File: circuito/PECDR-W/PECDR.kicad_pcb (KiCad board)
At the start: 4 copper layers, 85 x 54 mm, 68 parts, among them J1 O2, J10 GP-SPI, J11 GP-SPI, J12 O3, J13 GND, J14 A, J15 B, J16 VS-SELECT, J17 GP-I2C1, J2 O4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

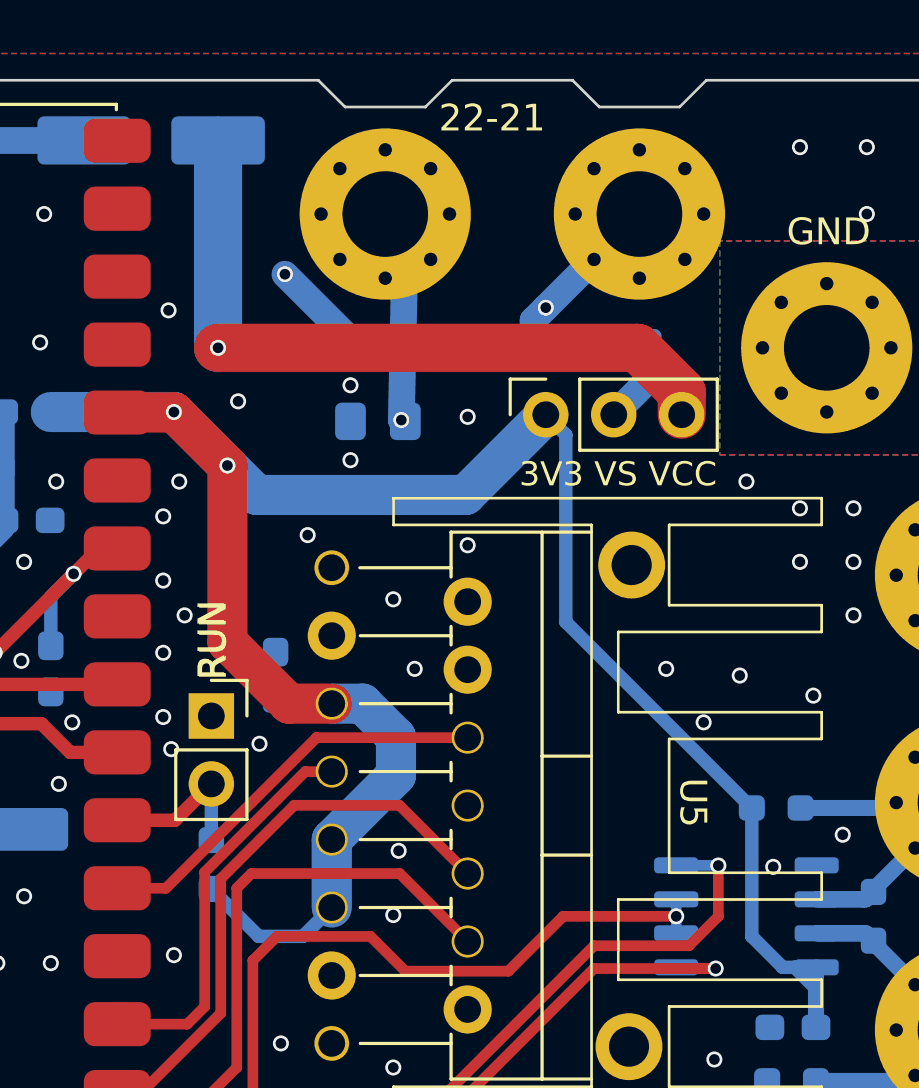
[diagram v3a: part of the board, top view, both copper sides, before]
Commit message: correção de layout e conexões no circuito PECDR-W
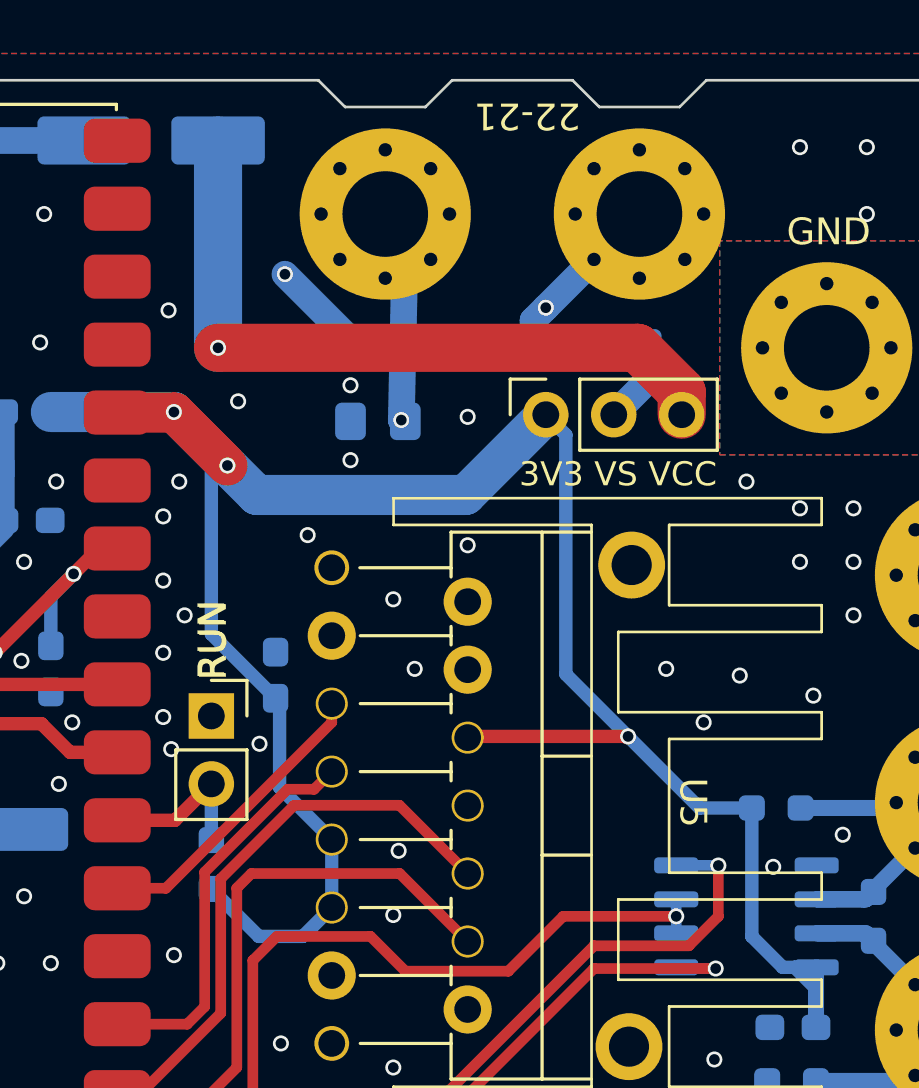
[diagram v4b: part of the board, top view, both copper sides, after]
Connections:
- U5 pad 5: +3V3 -> /GP22
- U5 pad 6: /GP22 -> +3V3
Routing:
- net /GP22: track 15.4 -> 11.3 mm
- net +3V3: track 227.5 -> 231.5 mm, vias 3 -> 4
